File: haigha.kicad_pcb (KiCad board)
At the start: 2 copper layers, 114.4 x 88.3 mm, 20 parts, among them J1 MJ-4PP-9, SW10 SW_PUSH, SW11 SW_PUSH, SW12 SW_PUSH, SW14 SW_PUSH, SW15 SW_PUSH, SW16 SW_PUSH, SW17 SW_PUSH, SW18 SW_PUSH, SW2 SW_PUSH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

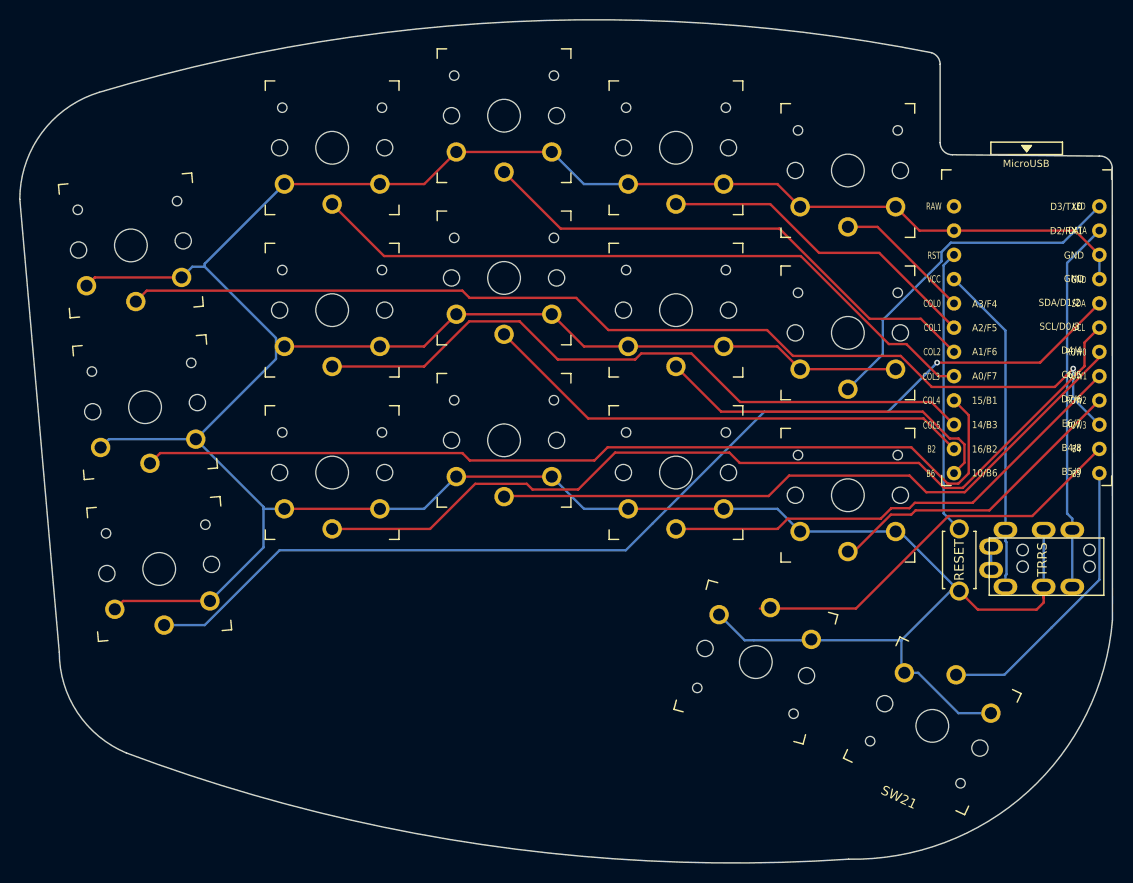
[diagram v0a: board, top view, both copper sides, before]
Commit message: modified haigha along with gerber file
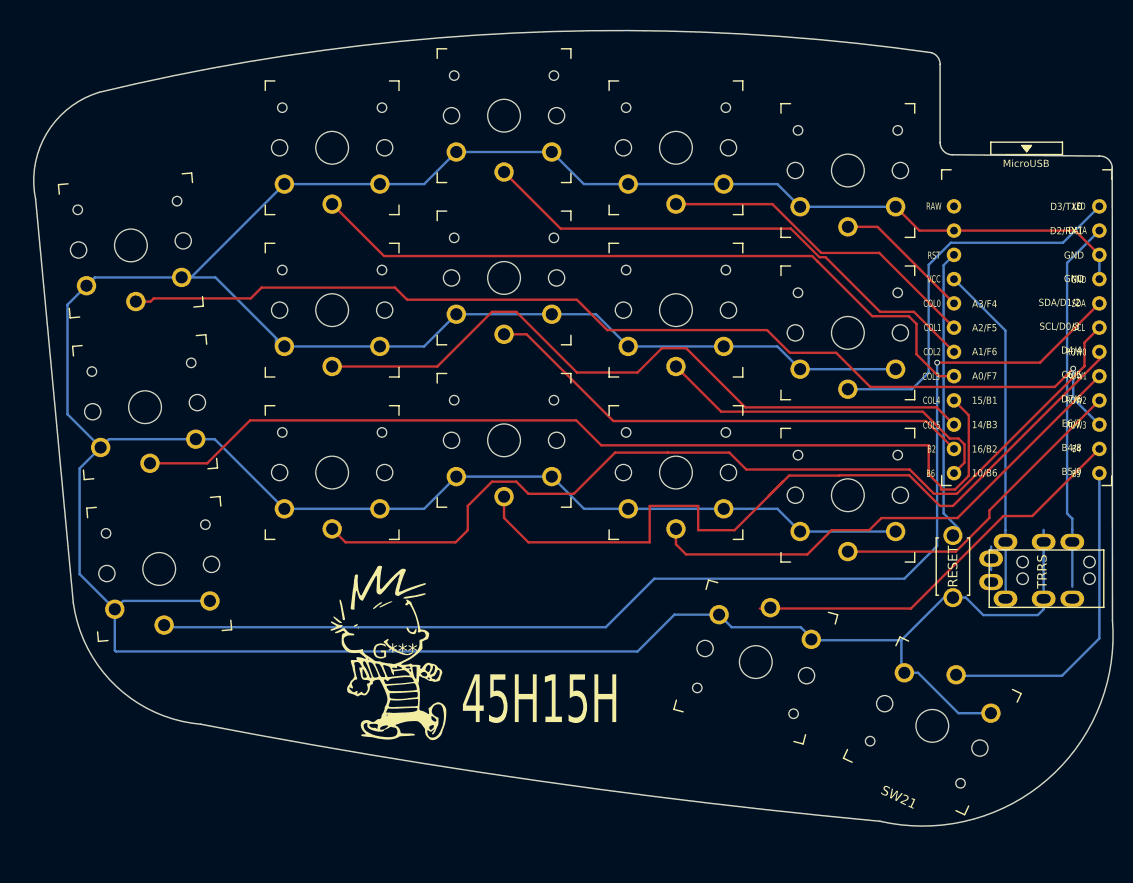
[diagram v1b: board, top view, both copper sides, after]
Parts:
- added G***: LOGO, calvin:calvin, F.Cu at (68.6, 81.3)
- moved J1 1.26 mm to (142.8, 73.7)
- moved RSW1 0.95 mm to (127.0, 72.4)
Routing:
- net GND: track 396.9 -> 471.6 mm
- net row0: track 70.4 -> 85.1 mm
- net SDA: track 111.9 -> 123.3 mm
- net col4: track 97.4 -> 101.7 mm
- net LED: track 36.9 -> 40.9 mm
- net SCL: track 94.1 -> 97.8 mm
- net Net-(U1-Pad12): track 30.3 -> 34.0 mm
- net row1: track 51.0 -> 54.1 mm
- net col5: track 72.1 -> 74.5 mm
- net col3: track 72.6 -> 74.4 mm
- net VCC: track 34.5 -> 35.8 mm
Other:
- board size 114.4 x 88.3 mm -> 113 x 83.3 mm
- net class Default removed
- board text added: "45H15H"

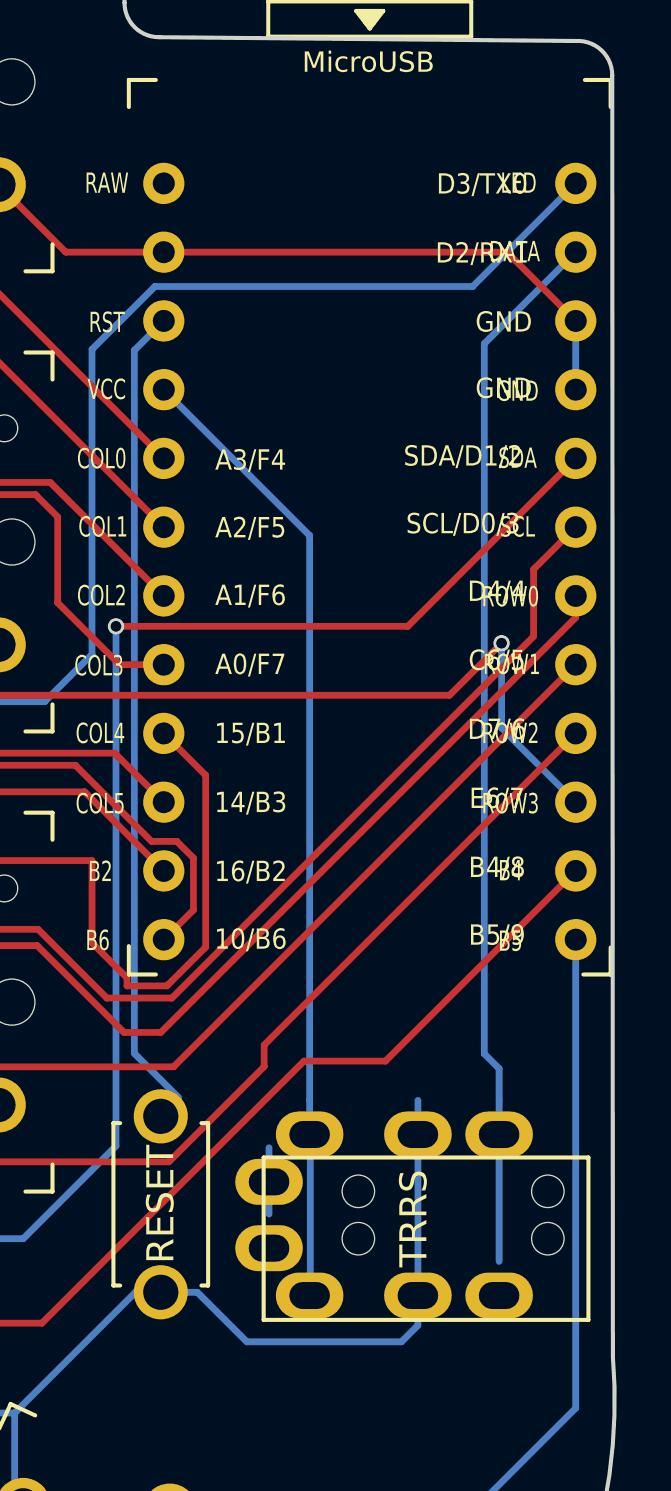
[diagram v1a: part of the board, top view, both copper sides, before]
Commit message: fix data trrs connection
clean microcontroller pin labels
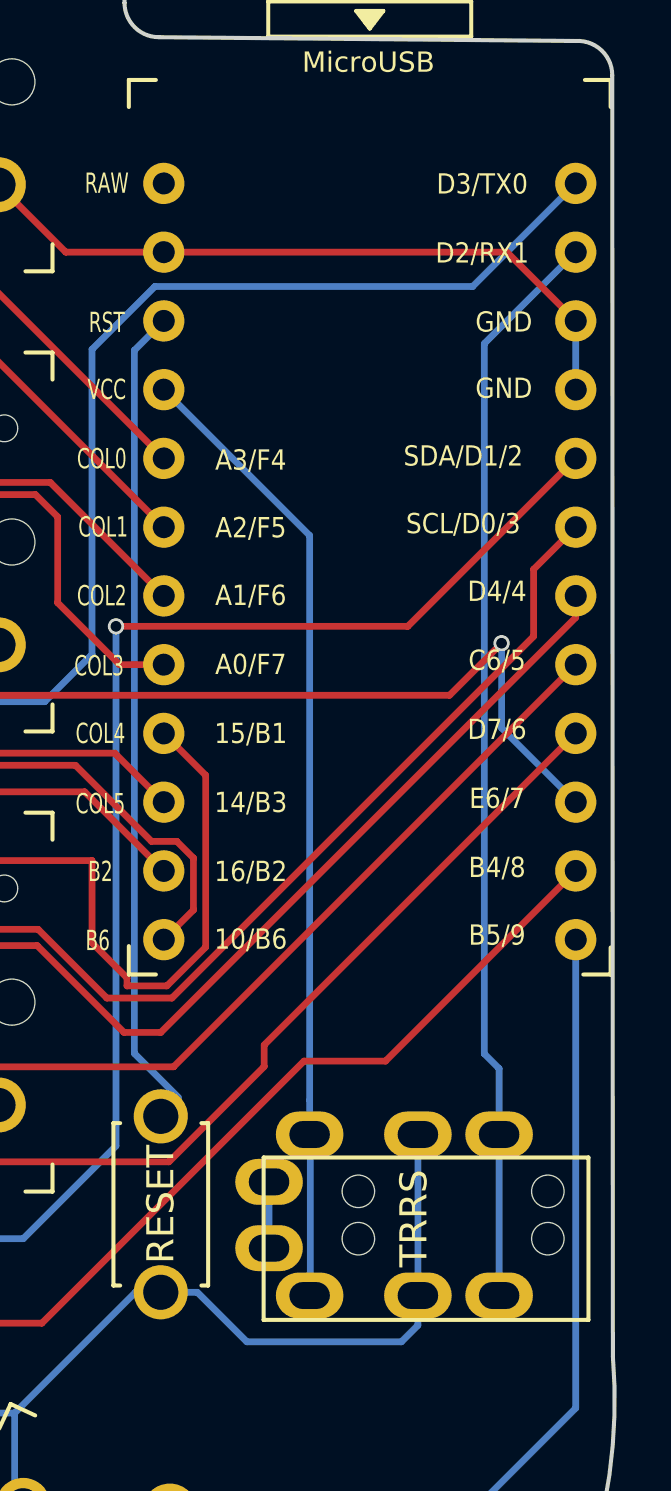
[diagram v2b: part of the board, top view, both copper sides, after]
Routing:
- net data: track 38.9 -> 40.2 mm
- net GND: track 471.6 -> 470.4 mm
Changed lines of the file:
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@@
     (pad_to_mask_clearance 0.2)
     (aux_axis_origin 145.73 12.66)
+    (grid_origin 69.85 81.28)
     (pcbplotparams
       (layerselection 0x00010fc_ffffffff)
@@
       (effects (font (size 0.75 0.67) (thickness 0.125)))
     )
-    (fp_text user "ROW1" (at 5.25 3.302) (layer "F.SilkS")
-      (effects (font (size 0.75 0.5) (thickness 0.125)))
-    )
     (fp_text user "COL4" (at -9.95 5.85) (layer "F.SilkS")
       (effects (font (size 0.75 0.5) (thickness 0.125)))
     )
-    (fp_text user "SCL" (at 5.461 -1.778) (layer "F.SilkS")
-      (effects (font (size 0.75 0.5) (thickness 0.125)))
-    )
     (fp_text user "A0/F7" (at -4.395 3.3 unlocked) (layer "F.SilkS")
       (effects (font (size 0.75 0.67) (thickness 0.125)))
     )
-    (fp_text user "DATA" (at 5.35 -11.95) (layer "F.SilkS")
-      (effects (font (size 0.75 0.5) (thickness 0.125)))
-    )
     (fp_text user "A1/F6" (at -4.395 0.75 unlocked) (layer "F.SilkS")
       (effects (font (size 0.75 0.67) (thickness 0.125)))
@@
       (effects (font (size 0.75 0.67) (thickness 0.125)))
     )
-    (fp_text user "LED" (at 5.5 -14.478) (layer "F.SilkS")
-      (effects (font (size 0.75 0.5) (thickness 0.125)))
-    )
     (fp_text user "D4/4" (at 4.705 0.6 unlocked) (layer "F.SilkS")
       (effects (font (size 0.75 0.67) (thickness 0.125)))
@@
       (effects (font (size 0.75 0.67) (thickness 0.125)))
     )
-    (fp_text user "B5" (at 5.2 13.5255) (layer "F.SilkS")
-      (effects (font (size 0.75 0.5) (thickness 0.125)))
-    )
     (fp_text user "MicroUSB" (at -0.05 -18.95) (layer "F.SilkS")
       (effects (font (size 0.75 0.75) (thickness 0.12)))
     )
-    (fp_text user "ROW3" (at 5.2 8.4455) (layer "F.SilkS")
-      (effects (font (size 0.75 0.5) (thickness 0.125)))
-    )
     (fp_text user "14/B3" (at -4.395 8.4 unlocked) (layer "F.SilkS")
       (effects (font (size 0.75 0.67) (thickness 0.125)))
@@
       (effects (font (size 0.75 0.67) (thickness 0.125)))
     )
-    (fp_text user "ROW0" (at 5.2 0.8) (layer "F.SilkS")
-      (effects (font (size 0.75 0.5) (thickness 0.125)))
-    )
-    (fp_text user "ROW2" (at 5.2 5.85) (layer "F.SilkS")
-      (effects (font (size 0.75 0.5) (thickness 0.125)))
-    )
     (fp_text user "16/B2" (at -4.395 10.95 unlocked) (layer "F.SilkS")
       (effects (font (size 0.75 0.67) (thickness 0.125)))
@@
       (effects (font (size 0.75 0.67) (thickness 0.125)))
     )
-    (fp_text user "B4" (at 5.2 10.922) (layer "F.SilkS")
-      (effects (font (size 0.75 0.5) (thickness 0.125)))
-    )
     (fp_text user "COL2" (at -9.9 0.762) (layer "F.SilkS")
       (effects (font (size 0.75 0.5) (thickness 0.125)))
@@
       (effects (font (size 0.75 0.67) (thickness 0.125)))
     )
-    (fp_text user "SDA" (at 5.461 -4.318) (layer "F.SilkS")
-      (effects (font (size 0.75 0.5) (thickness 0.125)))
-    )
-    (fp_text user "GND" (at 5.461 -6.7945 unlocked) (layer "F.SilkS")
-      (effects (font (size 0.75 0.5) (thickness 0.125)))
-    )
     (fp_text user "SCL/D0/3" (at 3.455 -1.9 unlocked) (layer "F.SilkS")
       (effects (font (size 0.75 0.67) (thickness 0.125)))
@@
   (segment (start 142.3314 39.752) (end 139.7914 37.212) (width 0.25) (layer "F.Cu") (net 6))
   (segment (start 71.625 66.345) (end 67 66.345) (width 0.25) (layer "B.Cu") (net 6))
-  (segment (start 121.5999 80.1036) (end 126.0635 75.64) (width 0.25) (layer "B.Cu") (net 6))
   (segment (start 34.29 56.449901) (end 34.29 44.974637) (width 0.25) (layer "B.Cu") (net 6))
   (segment (start 75 28.98) (end 85 28.98) (width 0.25) (layer "B.Cu") (net 6))
@@
   (segment (start 57 66.345) (end 67 66.345) (width 0.25) (layer "B.Cu") (net 6))
   (segment (start 88.36 32.34) (end 93 32.34) (width 0.25) (layer "B.Cu") (net 6))
-  (segment (start 135.89 77.47) (end 136.5 76.86) (width 0.25) (layer "B.Cu") (net 6))
   (segment (start 49.773861 42.113861) (end 57 49.34) (width 0.25) (layer "B.Cu") (net 6))
   (segment (start 35.56 73.178101) (end 35.56 62.121537) (width 0.25) (layer "B.Cu") (net 6))
@@
   (segment (start 121.91441 83.512939) (end 123.35125 83.512939) (width 0.25) (layer "B.Cu") (net 6))
   (segment (start 93 49.34) (end 103 49.34) (width 0.25) (layer "B.Cu") (net 6))
+  (segment (start 136.5 76.86) (end 136.5 69.81) (width 0.25) (layer "B.Cu") (net 6))
+  (segment (start 128.35 75.64) (end 130.18 77.47) (width 0.25) (layer "B.Cu") (net 6))
+  (segment (start 121.5999 80.1036) (end 126.0635 75.64) (width 0.25) (layer "B.Cu") (net 6))
   (segment (start 37.150776 42.113861) (end 36.279218 42.985419) (width 0.25) (layer "B.Cu") (net 6))
   (segment (start 85 28.98) (end 88.36 32.34) (width 0.25) (layer "B.Cu") (net 6))
@@
   (segment (start 46.241165 42.113861) (end 49.773861 42.113861) (width 0.25) (layer "B.Cu") (net 6))
   (segment (start 57 32.34) (end 67 32.34) (width 0.25) (layer "B.Cu") (net 6))
-  (segment (start 128.35 75.64) (end 130.18 77.47) (width 0.25) (layer "B.Cu") (net 6))
   (segment (start 89.63 45.97) (end 93 49.34) (width 0.25) (layer "B.Cu") (net 6))
   (segment (start 40.114476 75.989461) (end 49.204865 75.989461) (width 0.25) (layer "B.Cu") (net 6))
   (segment (start 111 34.72) (end 121 34.72) (width 0.25) (layer "B.Cu") (net 6))
   (segment (start 97.834613 77.425387) (end 102.513883 77.425387) (width 0.25) (layer "B.Cu") (net 6))
+  (segment (start 130.18 77.47) (end 135.89 77.47) (width 0.25) (layer "B.Cu") (net 6))
+  (segment (start 135.89 77.47) (end 136.5 76.86) (width 0.25) (layer "B.Cu") (net 6))
   (segment (start 103 32.34) (end 108.62 32.34) (width 0.25) (layer "B.Cu") (net 6))
   (segment (start 121.5999 80.1036) (end 112.4367 80.1036) (width 0.25) (layer "B.Cu") (net 6))
-  (segment (start 136.5 76.86) (end 136.5 68.55) (width 0.25) (layer "B.Cu") (net 6))
   (segment (start 88.375 66.345) (end 93 66.345) (width 0.25) (layer "B.Cu") (net 6))
   (segment (start 108.625 66.345) (end 111 68.72) (width 0.25) (layer "B.Cu") (net 6))
@@
   (segment (start 36.084637 43.18) (end 36.279218 42.985419) (width 0.25) (layer "B.Cu") (net 6))
   (segment (start 38.6323 59.0492) (end 37.7608 59.9207) (width 0.25) (layer "B.Cu") (net 6))
-  (segment (start 130.18 77.47) (end 135.89 77.47) (width 0.25) (layer "B.Cu") (net 6))
   (segment (start 127.577433 87.739122) (end 130.977488 87.739122) (width 0.25) (layer "B.Cu") (net 6))
   (segment (start 121.5999 83.198429) (end 121.91441 83.512939) (width 0.25) (layer "B.Cu") (net 6))
@@
   (segment (start 39.37 81.28) (end 93.98 81.28) (width 0.25) (layer "B.Cu") (net 6))
   (segment (start 34.29 44.974637) (end 36.279218 42.985419) (width 0.25) (layer "B.Cu") (net 6))
+  (segment (start 126.0635 75.64) (end 128.35 75.64) (width 0.25) (layer "B.Cu") (net 6))
   (segment (start 142.3314 39.752) (end 142.3314 42.292) (width 0.25) (layer "B.Cu") (net 6))
   (segment (start 93 66.345) (end 103 66.345) (width 0.25) (layer "B.Cu") (net 6))
@@
   (segment (start 103 66.345) (end 108.625 66.345) (width 0.25) (layer "B.Cu") (net 6))
   (segment (start 35.56 43.18) (end 36.084637 43.18) (width 0.25) (layer "B.Cu") (net 6))
-  (segment (start 126.0635 75.64) (end 128.35 75.64) (width 0.25) (layer "B.Cu") (net 6))
   (segment (start 111 68.72) (end 121 68.72) (width 0.25) (layer "B.Cu") (net 6))
   (segment (start 47.7228 59.0492) (end 38.6323 59.0492) (width 0.25) (layer "B.Cu") (net 6))
@@
   (segment (start 122.71 53.82) (end 124.46 52.07) (width 0.25) (layer "B.Cu") (net 13))
   (segment (start 126.7802 38.482) (end 138.5214 38.482) (width 0.25) (layer "B.Cu") (net 13))
-  (segment (start 139.5 74.5) (end 139.5 68.55) (width 0.25) (layer "B.Cu") (net 14))
-  (segment (start 139.5 68.55) (end 139.5 67.3747) (width 0.25) (layer "B.Cu") (net 14))
+  (segment (start 139.5 69.81) (end 139.5 67.3747) (width 0.25) (layer "B.Cu") (net 14))
+  (segment (start 139.5 69.81) (end 139.5 75.76) (width 0.25) (layer "B.Cu") (net 14))
+  (segment (start 138.9537 66.8284) (end 138.9537 40.5897) (width 0.25) (layer "B.Cu") (net 14))
   (segment (start 139.5 67.3747) (end 138.9537 66.8284) (width 0.25) (layer "B.Cu") (net 14))
   (segment (start 138.9537 40.5897) (end 142.3314 37.212) (width 0.25) (layer "B.Cu") (net 14))
-  (segment (start 138.9537 66.8284) (end 138.9537 40.5897) (width 0.25) (layer "B.Cu") (net 14))
   (segment (start 126.024 40.8394) (end 127.1114 39.752) (width 0.25) (layer "B.Cu") (net 15))
   (segment (start 126.024 66.814) (end 126.024 40.8394) (width 0.25) (layer "B.Cu") (net 15))
@@
   (segment (start 122.609 76.781) (end 132.2912 67.0988) (width 0.25) (layer "F.Cu") (net 21))
   (segment (start 135.3046 67.0988) (end 142.3314 60.072) (width 0.25) (layer "F.Cu") (net 21))
-  (segment (start 131 72.75) (end 131 70.3) (width 0.25) (layer "B.Cu") (net 22))
+  (segment (start 131 74.01) (end 131 71.56) (width 0.25) (layer "B.Cu") (net 22))
 )
